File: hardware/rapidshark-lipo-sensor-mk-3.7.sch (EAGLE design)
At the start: 26 parts, among them Q1 IRLML2244, Q2 IRLML2502, Q3 IRLML2244, Q4 IRLML2502, Q5 IRLML2244, Q6 IRLML2502, U1 Tiny84

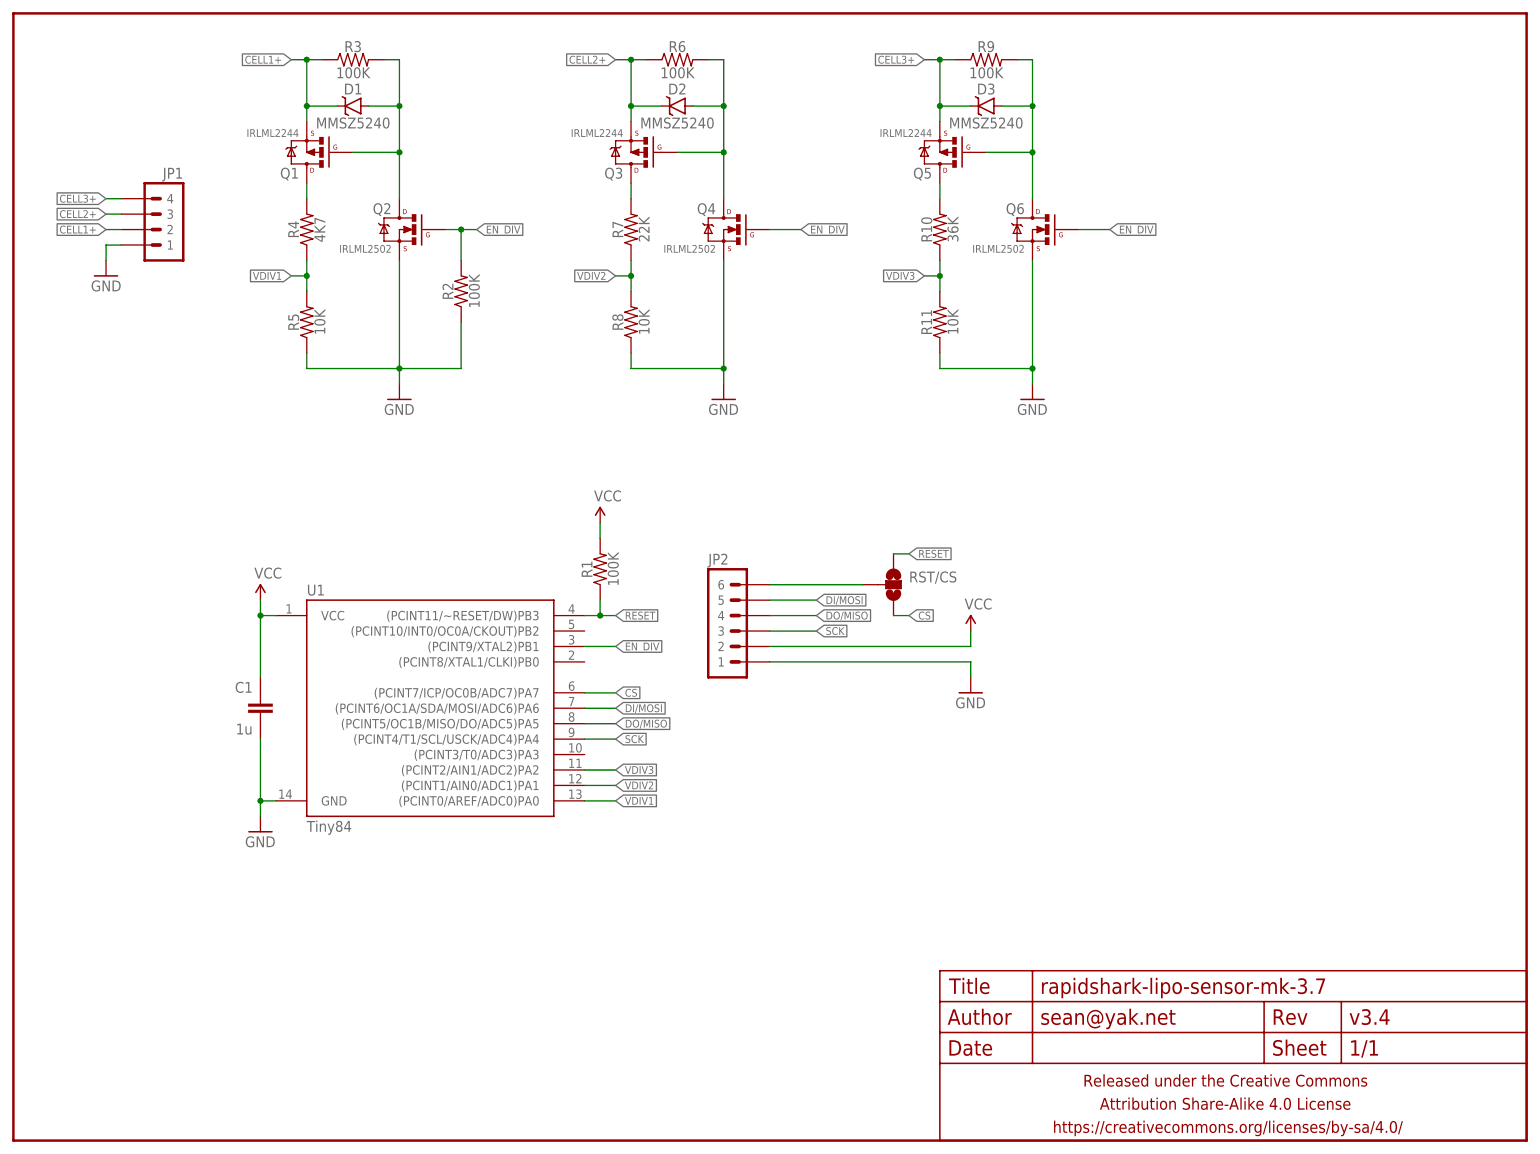
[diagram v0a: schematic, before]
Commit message: lipo sensors suck
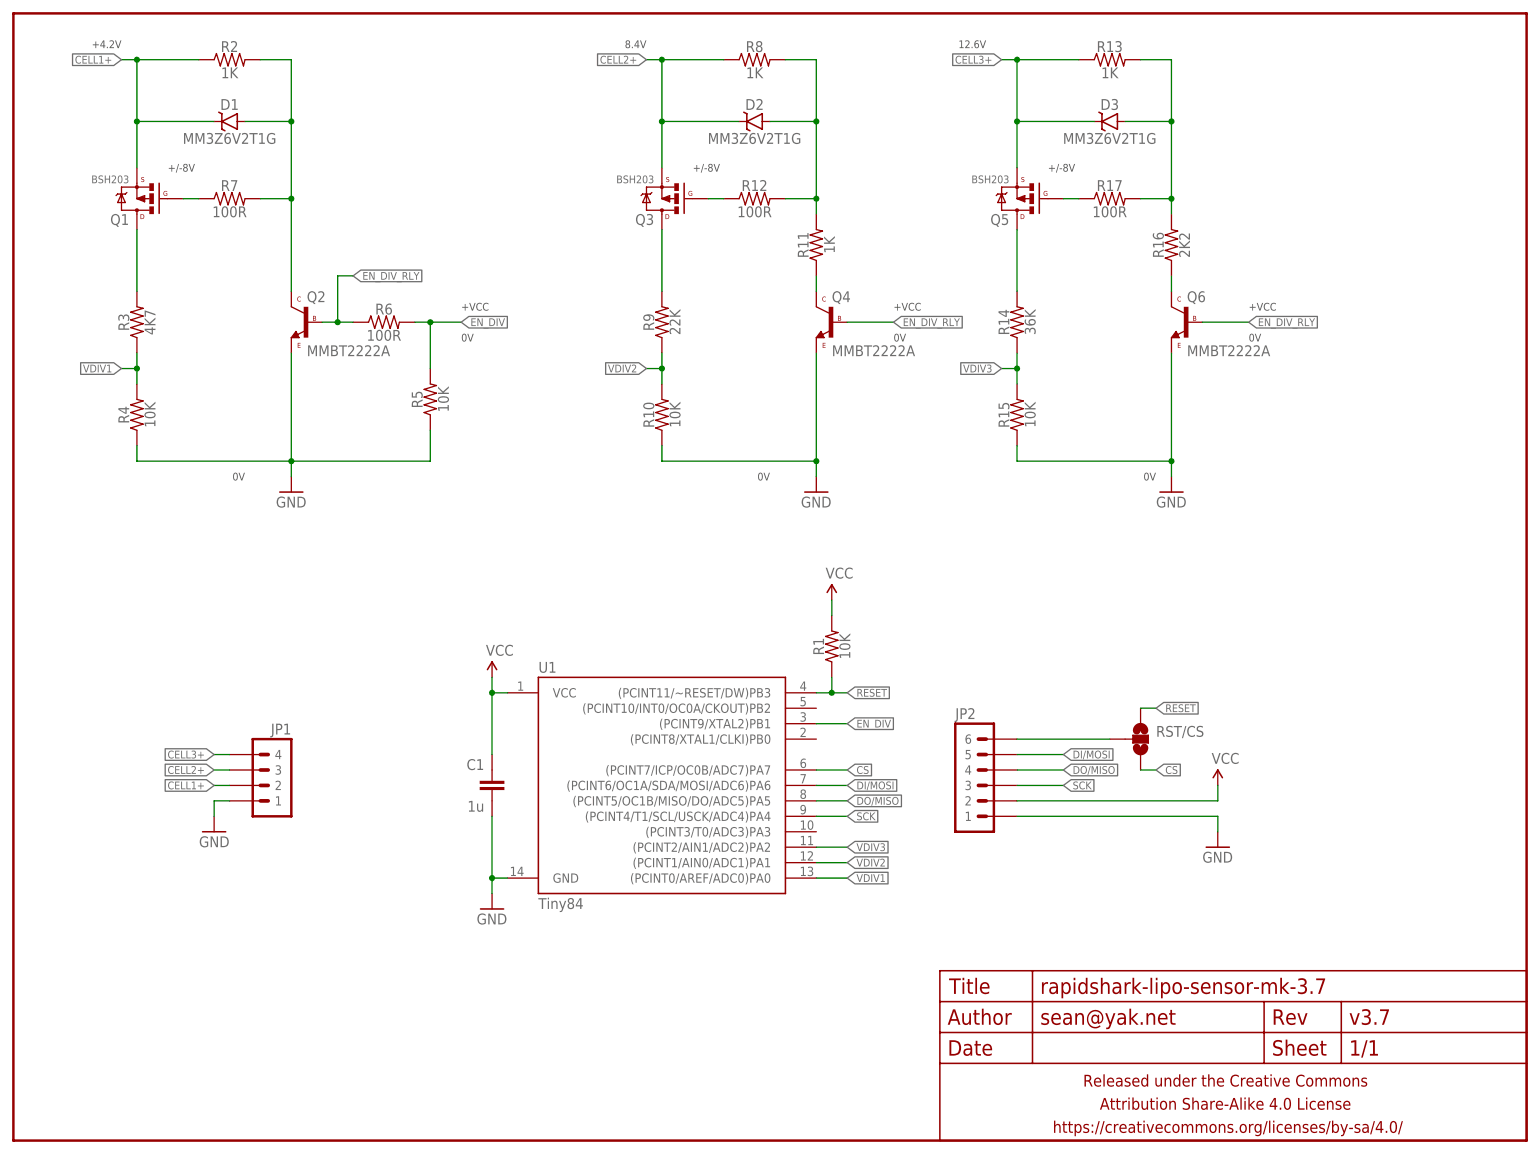
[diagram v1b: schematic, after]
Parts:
- added R12, R17: 100R, a_parts:RESISTORR0603-TIGHTER
- added R13: 1K, a_parts:RESISTORR0603-TIGHTER
- added R14: 36K, a_parts:RESISTORR0603-TIGHTER
- added R15: 10K, a_parts:RESISTORR0603-TIGHTER
- added R16: 2K2, a_parts:RESISTORR0603-TIGHTER
- D1, D2, D3: value MMSZ5240 -> MM3Z6V2T1G; device a_parts:DIODE-ZENERSOD123 -> a_parts:DIODE-ZENERSOD323
- FRAME1: VERSION v3.4 -> v3.7
- Q1, Q3, Q5: value IRLML2244 -> BSH203
- Q2, Q4, Q6: value IRLML2502 -> MMBT2222A; device a_parts:MOSFET-NCHANNELIRLML2502 -> a_parts:TRANSISTOR_NPNMMBT2222A
- R1: value 100K -> 10K
- R10: value 36K -> 10K
- R11, R8: value 10K -> 1K
- R2: value 100K -> 1K
- R3: value 100K -> 4K7
- R4: value 4K7 -> 10K
- R6: value 100K -> 100R
- R7: value 22K -> 100R
- R9: value 100K -> 22K
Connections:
- removed net N$4: D1.A, Q1.G, Q2.D, R3.2
- new net EN_DIV_RLY: Q2.B, Q4.B, Q6.B, R6.1
- new net N$1: Q4.C, R11.1
- new net N$10: Q1.G, R7.1
- new net N$11: Q3.G, R12.1
- new net N$12: Q5.G, R17.1
- new net N$8: Q6.C, R16.1
- new net N$9: D1.A, Q2.C, R2.2, R7.2
- net CELL1+: now also R2.1; no longer R3.1
- net CELL2+: now also R8.1; no longer R6.1
- net CELL3+: now also R13.1; no longer R9.1
- net EN_DIV: now also R5.2, R6.2; no longer Q2.G, Q4.G, Q6.G, R2.2
- net GND: now also Q2.E, Q4.E, Q6.E, R10.1, R15.1, R4.1; no longer Q2.S, Q4.S, Q6.S, R11.1, R2.1, R8.1
- net N$2: now also R9.2; no longer R7.2
- net N$3: now also R14.2; no longer R10.2
- net N$5: now also R11.2, R12.2, R8.2; no longer Q3.G, Q4.D, R6.2
- net N$6: now also R3.2; no longer R4.2
- net N$7: now also R13.2, R16.2, R17.2; no longer Q5.G, Q6.D, R9.2
- net VDIV1: now also R3.1, R4.2; no longer R4.1, R5.2
- net VDIV2: now also R10.2, R9.1; no longer R7.1, R8.2
- net VDIV3: now also R14.1, R15.2; no longer R10.1, R11.2
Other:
- note added: "+/-8V"
- note added: "+4.2V"
- note added: "+VCC"
- note added: "0V"
- note added: "12.6V"
- note added: "8.4V"
- moved on the sheet: C1, D1, D2, D3, JP1, JP2, Q1, Q3, Q5, R1, R10, R11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

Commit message: oh hey more hardware fails
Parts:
- removed R12, R17, R7: 100R, a_parts:RESISTORR0603-TIGHTER
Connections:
- removed net N$10: Q1.G, R7.1
- removed net N$11: Q3.G, R12.1
- removed net N$12: Q5.G, R17.1
- net N$5: now also Q3.G; no longer R12.2
- net N$7: now also Q5.G; no longer R17.2
- net N$9: now also Q1.G; no longer R7.2
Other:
- moved on the sheet: D1, D2, D3, Q1, Q2, Q3, Q4, Q5, Q6, R10, R11, R13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
